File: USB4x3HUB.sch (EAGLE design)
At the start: 117 parts, among them IC1 TUSB2036, IC10 SN74LVC1G139DCTR, IC2 FSUSB74MPX, IC3 TPS2041C, IC4 TPS2041C, IC5 TPS2041C, IC6 3.3V, IC7 5V, IC8 5V, IC9 5V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

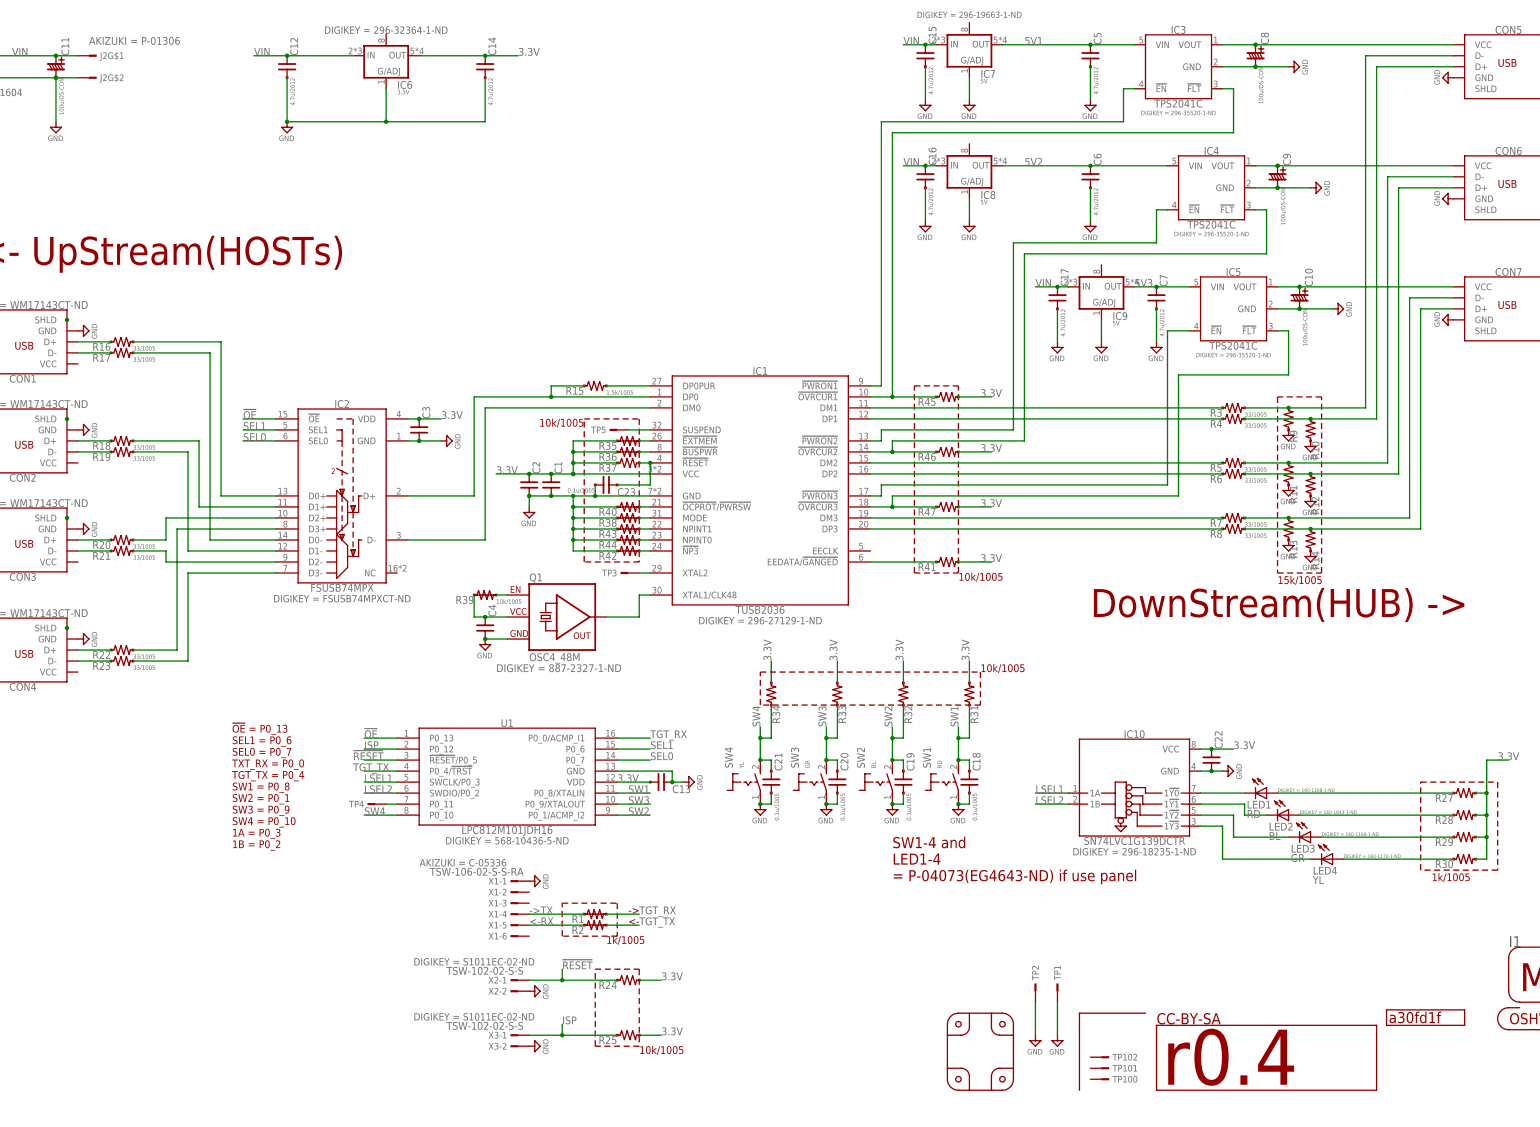
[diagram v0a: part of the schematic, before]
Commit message: [ PCB ] start r0.5 develop
- remove GND terminal(TP1)
- move switches and microB to south
  - some silk move regards to this
- move DC jack to face on microB side
- future: microB move to bottom side, and replace switch to panel type?
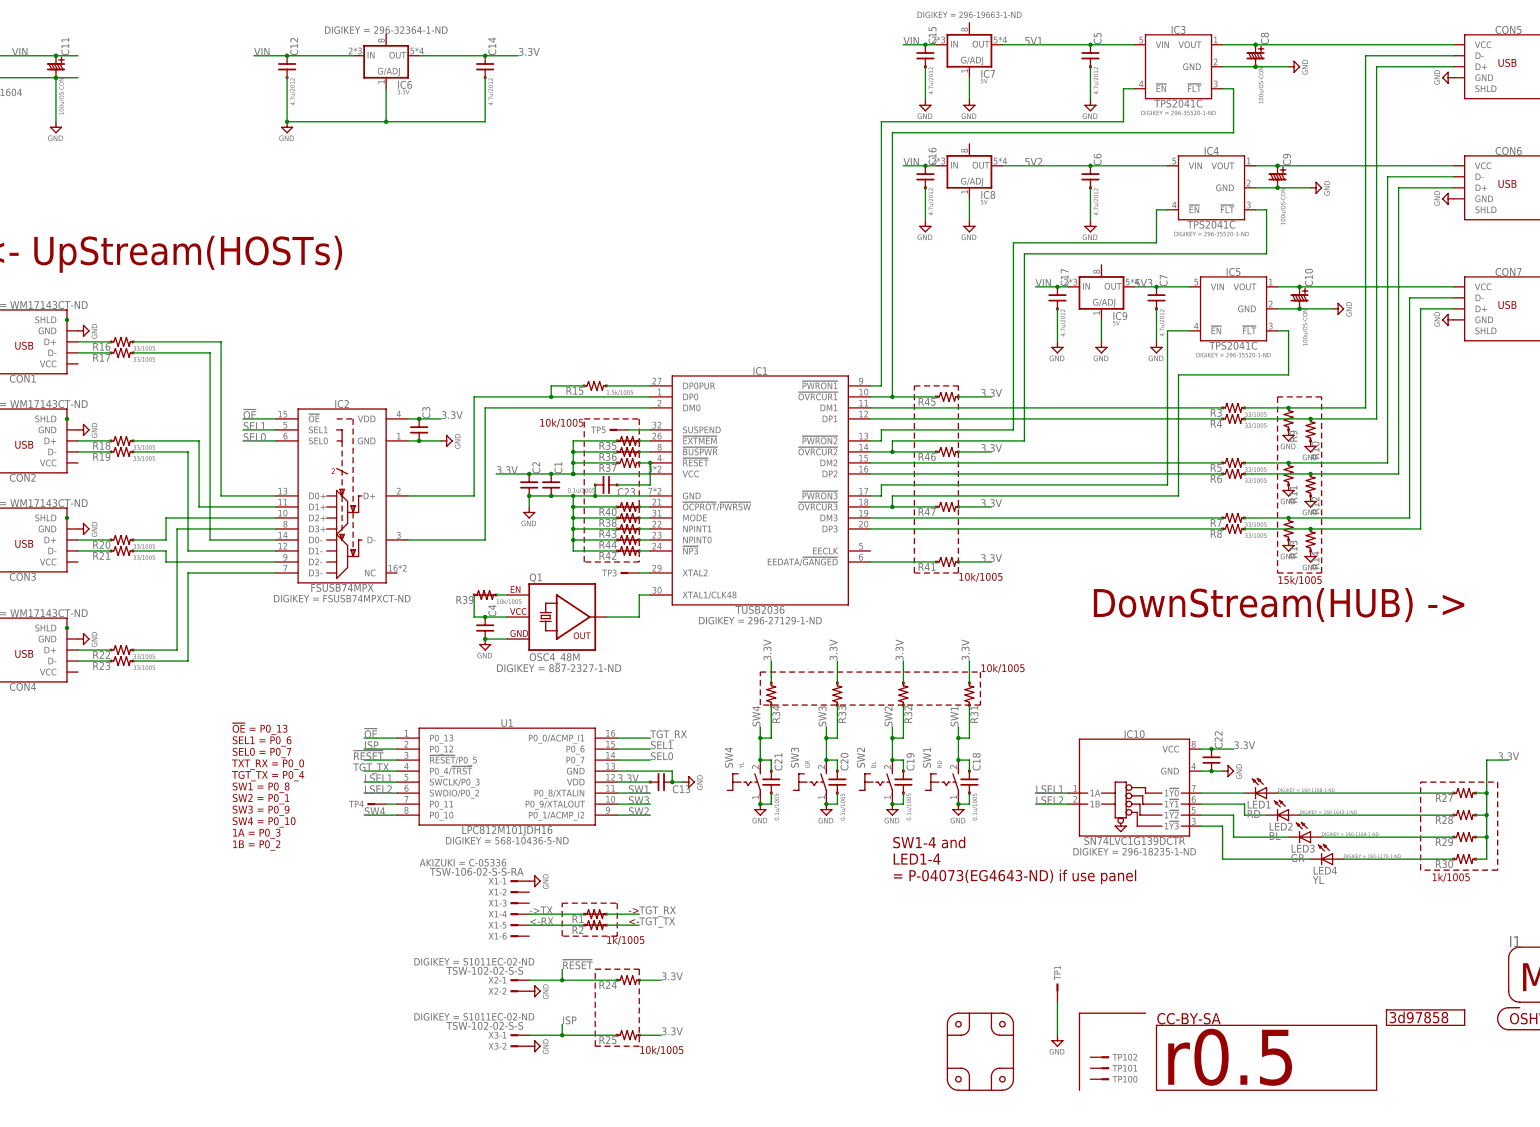
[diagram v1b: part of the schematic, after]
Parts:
- removed J2: (no value), mylib:TB111-2-2-U-1-1
- removed TP2: (no value), mylib:TESTPAD_4020
- GIT1: value a30fd1f -> 3d97858
- ICON2: value r0.4 -> r0.5
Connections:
- net GND: no longer J2G$2.1, TP2.1
- net VIN: no longer J2G$1.1
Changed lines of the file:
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@@
 <part name="R32" library="mylib" deviceset="R_US_*" device="_1005" technology="10K"/>
 <part name="R31" library="mylib" deviceset="R_US_*" device="_1005" technology="10K"/>
-<part name="SUPPLY34" library="mylib" deviceset="GND" device=""/>
 <part name="SUPPLY35" library="mylib" deviceset="GND" device=""/>
 <part name="R35" library="mylib" deviceset="R_US_*" device="_1005SHORT"/>
@@
 <part name="TP102" library="mylib" deviceset="TESTPAD" device="_F"/>
 <part name="ICON1" library="mylib" deviceset="ICON_OSHW" device="" value="OSHW"/>
-<part name="ICON2" library="mylib" deviceset="ICON_REVISION" device="_2.0" value="r0.4"/>
-<part name="GIT1" library="git-revision" deviceset="GIT-REVISION" device="_1.0" value="a30fd1f"/>
+<part name="ICON2" library="mylib" deviceset="ICON_REVISION" device="_2.0" value="r0.5"/>
+<part name="GIT1" library="git-revision" deviceset="GIT-REVISION" device="_1.0" value="3d97858"/>
 <part name="TP1" library="mylib" deviceset="TESTPAD" device="_4020"/>
-<part name="TP2" library="mylib" deviceset="TESTPAD" device="_4020"/>
 <part name="R41" library="mylib" deviceset="R_US_*" device="_1005" technology="10K"/>
 <part name="R40" library="mylib" deviceset="R_US_*" device="_1005SHORT"/>
@@
 <part name="P3" library="mylib" deviceset="PCB_CORNER" device=""/>
 <part name="P4" library="mylib" deviceset="PCB_CORNER" device=""/>
-<part name="J2" library="mylib" deviceset="TB111-2-*" device="2-U-1-1"/>
 <part name="TP5" library="mylib" deviceset="TESTPAD" device=""/>
 </parts>
@@
 <instance part="R32" gate="G$1" x="231.14" y="96.52" rot="R90"/>
 <instance part="R31" gate="G$1" x="246.38" y="96.52" rot="R90"/>
-<instance part="SUPPLY34" gate="GND" x="261.62" y="15.24"/>
 <instance part="SUPPLY35" gate="GND" x="266.7" y="15.24"/>
 <instance part="R35" gate="G$1" x="167.64" y="154.94"/>
@@
 <instance part="GIT1" gate="G$1" x="342.9" y="20.32"/>
 <instance part="TP1" gate="1" x="266.7" y="27.94" rot="R90"/>
-<instance part="TP2" gate="1" x="261.62" y="27.94" rot="R90"/>
 <instance part="R41" gate="G$1" x="241.3" y="127"/>
 <instance part="R40" gate="G$1" x="167.64" y="139.7"/>
@@
 <instance part="P3" gate="G$1" x="246.38" y="10.16" rot="R270"/>
 <instance part="P4" gate="G$1" x="251.46" y="10.16"/>
-<instance part="J2" gate="G$1" x="43.18" y="243.84">
-<attribute name="AKIZUKI" x="43.18" y="246.38" size="1.778" layer="96" display="both"/>
-</instance>
-<instance part="J2" gate="G$2" x="43.18" y="238.76"/>
 <instance part="TP5" gate="1" x="165.1" y="157.48" rot="R180"/>
 </instances>
@@
 <wire x1="20.32" y1="243.84" x2="35.56" y2="243.84" width="0.1524" layer="91"/>
 <label x="25.4" y="243.84" size="1.778" layer="95"/>
-<pinref part="J2" gate="G$1" pin="1"/>
 <wire x1="40.64" y1="243.84" x2="35.56" y2="243.84" width="0.1524" layer="91"/>
 <junction x="35.56" y="243.84"/>
@@
 <wire x1="35.56" y1="228.6" x2="35.56" y2="238.76" width="0.1524" layer="91"/>
 <junction x="35.56" y="238.76"/>
-<pinref part="J2" gate="G$2" pin="1"/>
 <wire x1="35.56" y1="238.76" x2="40.64" y2="238.76" width="0.1524" layer="91"/>
 </segment>
@@
 </segment>
 <segment>
-<pinref part="SUPPLY34" gate="GND" pin="GND"/>
-<pinref part="TP2" gate="1" pin="1"/>
-<wire x1="261.62" y1="25.4" x2="261.62" y2="17.78" width="0.1524" layer="91"/>
-</segment>
-<segment>

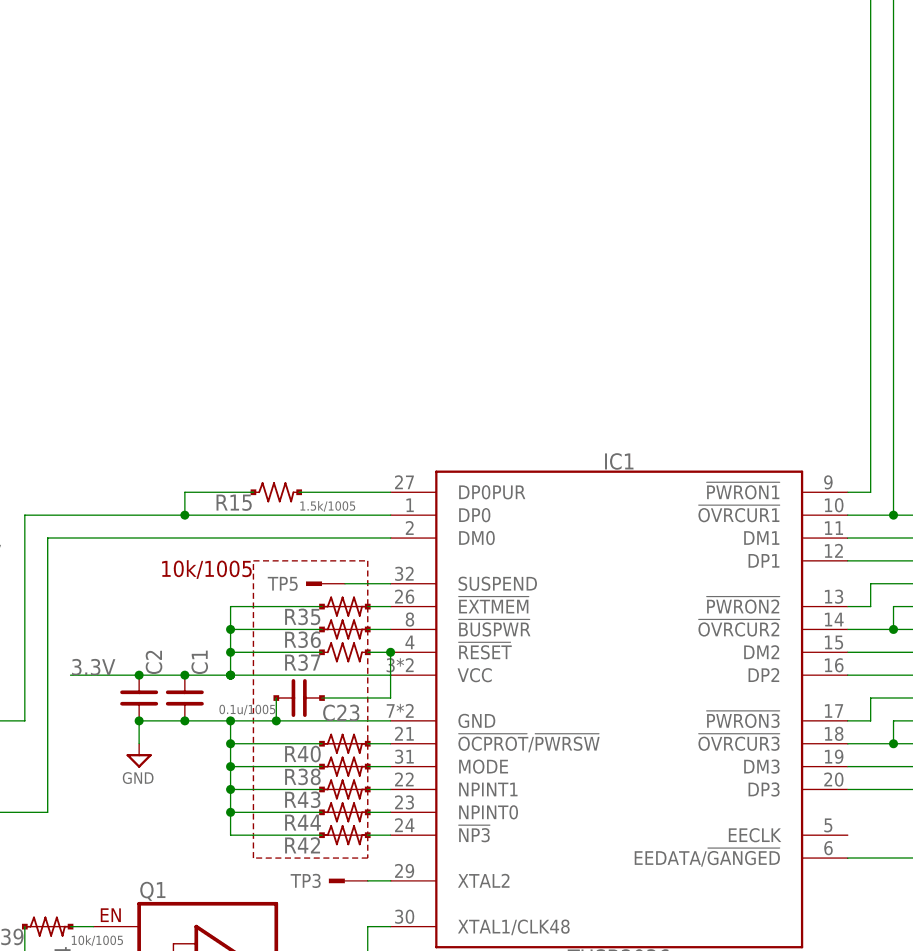
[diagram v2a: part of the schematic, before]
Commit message: [ BRD ] fix clock mode
- 48M source used while 6M source selected for IC
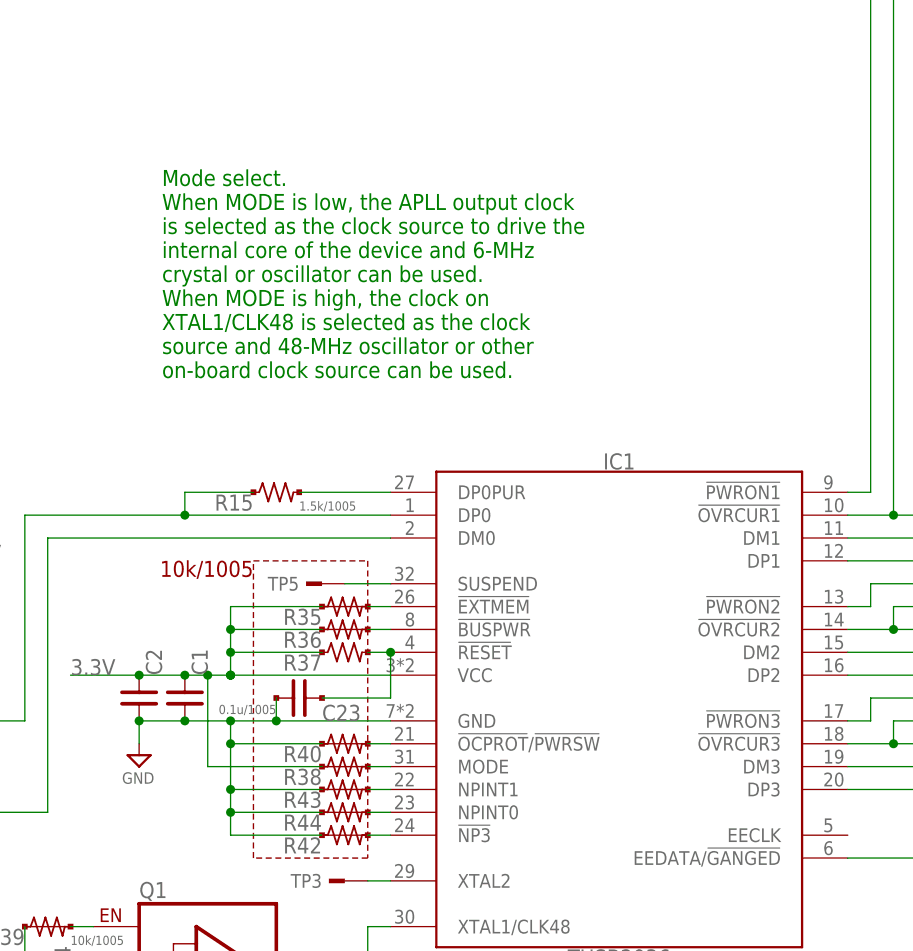
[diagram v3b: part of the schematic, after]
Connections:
- net 3.3V: now also R38.1
- net GND: no longer R38.1
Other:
- note added: "Mode select. When MODE is low, the APLL output clock is selected as the clock source to drive the internal core of the device and 6-MHz crystal or oscillator can be used. When MODE is high, the clock on XTAL1/CLK48 is selected as the clock source and 48-MHz oscillator or other on-board clock source can be used."
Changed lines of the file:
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@@
 <wire x1="157.48" y1="45.72" x2="162.56" y2="45.72" width="0.1524" layer="94"/>
 <wire x1="162.56" y1="43.18" x2="157.48" y2="43.18" width="0.1524" layer="94"/>
+<text x="147.32" y="180.34" size="1.778" layer="91">Mode select.
+When MODE is low, the APLL output clock
+is selected as the clock source to drive the
+internal core of the device and 6-MHz
+crystal or oscillator can be used.
+When MODE is high, the clock on
+XTAL1/CLK48 is selected as the clock
+source and 48-MHz oscillator or other
+on-board clock source can be used.</text>
 </plain>
 <instances>
@@
 <wire x1="154.94" y1="132.08" x2="154.94" y2="134.62" width="0.1524" layer="91"/>
 <junction x="154.94" y="142.24"/>
-<wire x1="154.94" y1="134.62" x2="154.94" y2="137.16" width="0.1524" layer="91"/>
-<wire x1="154.94" y1="137.16" x2="154.94" y2="139.7" width="0.1524" layer="91"/>
+<wire x1="154.94" y1="134.62" x2="154.94" y2="139.7" width="0.1524" layer="91"/>
 <wire x1="154.94" y1="139.7" x2="154.94" y2="142.24" width="0.1524" layer="91"/>
 <junction x="154.94" y="134.62"/>
@@
 <junction x="154.94" y="132.08"/>
 <junction x="154.94" y="139.7"/>
-<pinref part="R38" gate="G$1" pin="1"/>
 <wire x1="165.1" y1="139.7" x2="154.94" y2="139.7" width="0.1524" layer="91"/>
-<wire x1="165.1" y1="137.16" x2="154.94" y2="137.16" width="0.1524" layer="91"/>
-<junction x="154.94" y="137.16"/>
 <pinref part="R40" gate="G$1" pin="1"/>
 <pinref part="R43" gate="G$1" pin="1"/>
@@
 <label x="137.16" y="147.32" size="1.778" layer="95"/>
 <wire x1="144.78" y1="147.32" x2="149.86" y2="147.32" width="0.1524" layer="91"/>
-<wire x1="149.86" y1="147.32" x2="154.94" y2="147.32" width="0.1524" layer="91"/>
+<wire x1="149.86" y1="147.32" x2="152.4" y2="147.32" width="0.1524" layer="91"/>
+<wire x1="152.4" y1="147.32" x2="154.94" y2="147.32" width="0.1524" layer="91"/>
 <wire x1="154.94" y1="147.32" x2="172.72" y2="147.32" width="0.1524" layer="91"/>
 <junction x="154.94" y="147.32"/>
@@
 <junction x="154.94" y="149.86"/>
 <junction x="154.94" y="152.4"/>
-</segment>
-<segment>
+<wire x1="152.4" y1="147.32" x2="152.4" y2="137.16" width="0.1524" layer="91"/>
+<junction x="152.4" y="147.32"/>
+<pinref part="R38" gate="G$1" pin="1"/>
+<wire x1="152.4" y1="137.16" x2="165.1" y2="137.16" width="0.1524" layer="91"/>
+</segment>
+<segment>
